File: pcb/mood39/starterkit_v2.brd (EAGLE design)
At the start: 32 x 32 mm, 19 parts, among them IC1 TINY85, IC2 LP2950

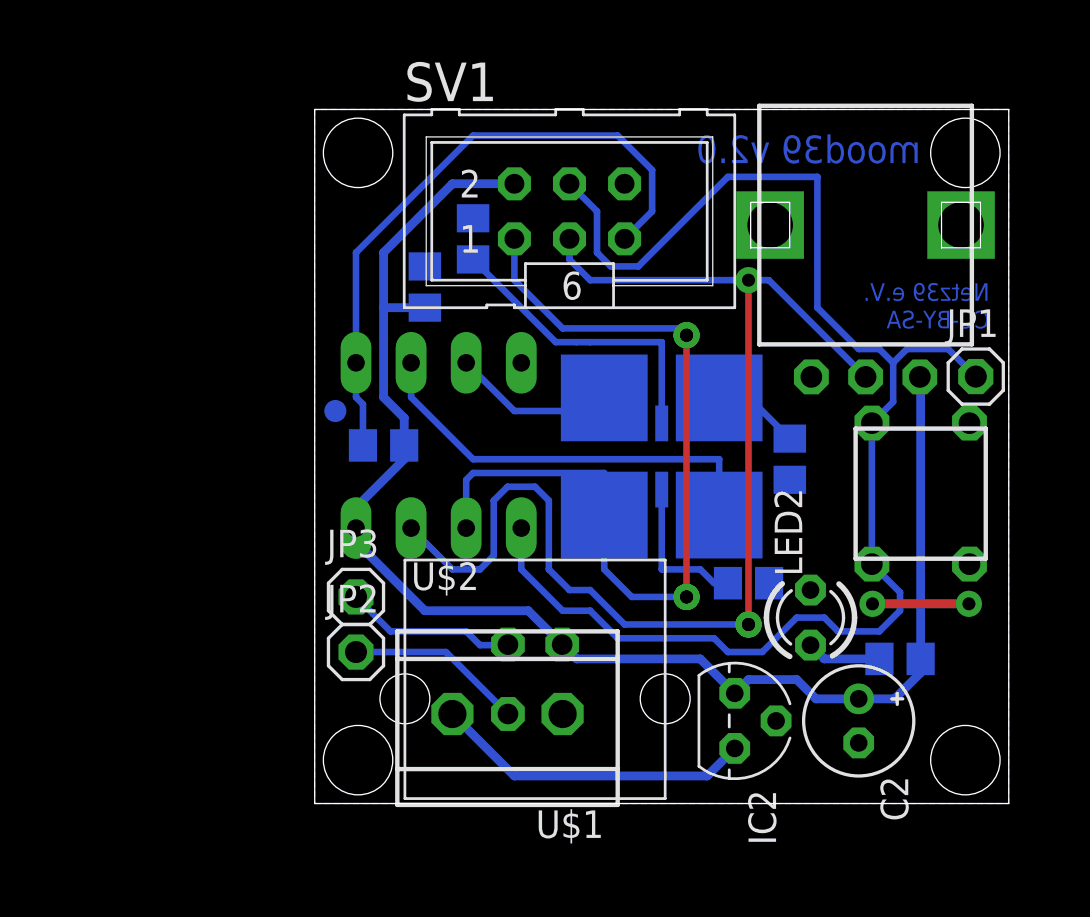
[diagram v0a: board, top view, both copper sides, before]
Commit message: move uC to top layer
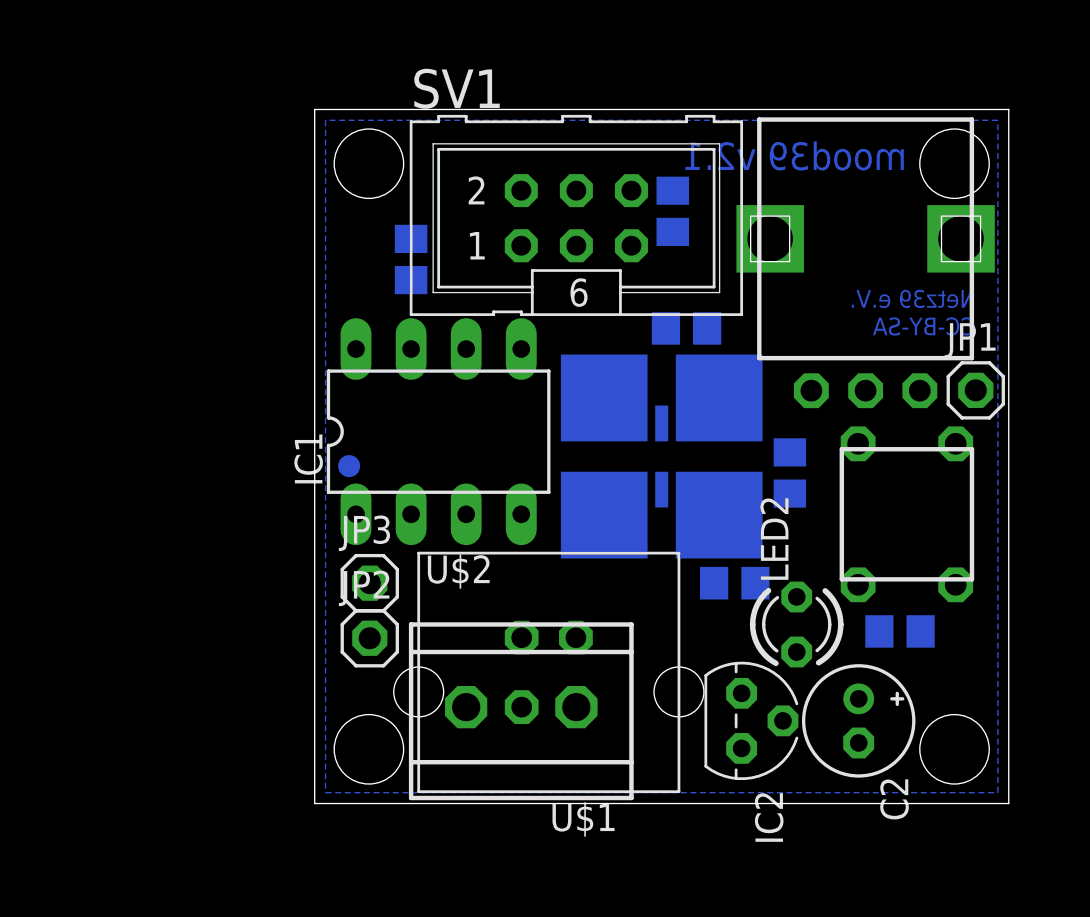
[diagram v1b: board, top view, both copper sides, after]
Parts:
- moved R1 17.2 mm to (16.5, 27.3), turned to 90 degrees
- moved R2 10.7 mm to (17.1, 21.9), turned to 180 degrees
- moved C1 1.42 mm to (4.45, 25.1)
- moved R6 1.27 mm to (27.0, 7.94)
- moved S1 1.14 mm to (27.3, 13.3)
- moved JP2 0.90 mm to (2.54, 7.62)
- moved JP3 0.90 mm to (2.54, 10.2)
- moved U$1 0.71 mm to (9.53, 4.45)
- moved U$2 0.71 mm to (10.8, 4.45)
- moved LED2 0.71 mm to (22.2, 8.26)
- moved R3 0.64 mm to (19.4, 10.2)
- moved R5 0.64 mm to (25.4, 26.0)
- moved R4 0.63 mm to (21.9, 15.2)
- moved IC1 0.63 mm to (5.71, 17.1), flipped to the top, turned to 0 degrees
- moved JP1 0.63 mm to (30.5, 19.1)
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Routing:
- net VCC: track 67.6 -> 0.00 mm
- net MOSI: track 65.6 -> 0.00 mm
- net SCK: track 56.6 -> 0.00 mm, vias 2 -> 0
- net MISO: track 41.7 -> 0.00 mm, vias 2 -> 0
- net !RESET: track 29.3 -> 0.00 mm
- net PB3: track 19.6 -> 0.00 mm
- net V+: track 14.7 -> 0.00 mm
- net N$5: track 14.0 -> 0.00 mm
- net USBD+: track 8.19 -> 0.00 mm
- net USBD-: track 7.94 -> 0.00 mm
- net PB4: track 7.54 -> 0.00 mm
- net N$6: track 7.00 -> 0.00 mm
- net GND: track 4.45 -> 0.00 mm, vias 2 -> 0
- net N$7: track 4.03 -> 0.00 mm
- net N$1: track 3.44 -> 0.00 mm
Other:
- board text added: "mood39 v2.1"
- board text removed: "mood39 v2.0"

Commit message: try another puzzle
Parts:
- moved JP1 28.6 mm to (1.91, 19.1)
- moved S1 22.9 mm to (4.45, 13.3)
- moved R6 20.7 mm to (6.99, 2.54)
- moved IC1 20.4 mm to (26.0, 15.9), turned to 180 degrees
- moved R5 18.4 mm to (6.99, 26.0)
- moved LED2 17.8 mm to (4.45, 7.62)
- moved JP2 9.44 mm to (9.53, 14.0)
- moved JP3 9.44 mm to (9.53, 16.5)
- moved SV1 8.26 mm to (20.3, 26.7)
- moved C2 5.41 mm to (28.6, 7.94), turned to 180 degrees
- moved IC2 4.45 mm to (24.1, 3.81), turned to 0 degrees
- moved C1 3.43 mm to (6.35, 22.2), turned to 0 degrees
- moved U$2 3.24 mm to (14.0, 5.08)
- moved U$1 3.24 mm to (12.7, 5.08)
- moved R1 1.27 mm to (15.2, 27.3), turned to 270 degrees
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
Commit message: new usb connector package
this will be puzzling not fun :-/
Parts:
- U$2: value USB_B -> USB_BS; device n39:USB_B_UP -> n39:USB_B_UP-S
- moved U$1 2.03 mm to (14.0, 6.67)
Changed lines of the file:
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@@
 <attribute name="REICHELT" value="TASTER 9305" x="4.445" y="13.335" size="1.778" layer="27" rot="R90" display="off"/>
 </element>
-<element name="U$1" library="n39" package="RIACON_101_2" value="RIACON_101_2" x="12.7" y="5.08" rot="R180">
-<attribute name="REICHELT" value="AKL 101-02" x="12.7" y="5.08" size="1.778" layer="27" rot="R180" display="off"/>
+<element name="U$1" library="n39" package="RIACON_101_2" value="RIACON_101_2" x="13.97" y="6.6675" rot="R180">
+<attribute name="REICHELT" value="AKL 101-02" x="13.97" y="6.6675" size="1.778" layer="27" rot="R180" display="off"/>
 </element>
 <element name="JP2" library="pinhead" package="1X01" value="" x="9.525" y="13.97"/>
 <element name="JP3" library="pinhead" package="1X01" value="" x="9.525" y="16.51"/>
-<element name="U$2" library="n39" package="USB_B_UP" value="USB_B" x="13.97" y="5.08">
+<element name="U$2" library="n39" package="USB_B_UP-S" value="USB_BS" x="13.97" y="5.08">
 <attribute name="REICHELT" value="USB BG" x="13.97" y="5.08" size="1.778" layer="27" display="off"/>
 </element>
@@
 <contactref element="U$2" pad="4"/>
 <contactref element="R5" pad="1"/>
-<wire x1="18.095" y1="22.225" x2="22.86" y2="27.94" width="0" layer="19" extent="16-16"/>
-<wire x1="22.225" y1="19.685" x2="18.095" y2="22.225" width="0" layer="19" extent="16-16"/>
-<wire x1="22.225" y1="14.925" x2="22.225" y2="19.685" width="0" layer="19" extent="16-16"/>
-<wire x1="20" y1="10.16" x2="22.225" y2="14.925" width="0" layer="19" extent="16-16"/>
-<wire x1="24.13" y1="5.715" x2="20" y2="10.16" width="0" layer="19" extent="16-16"/>
-<wire x1="27.559" y1="7.9375" x2="24.13" y2="5.715" width="0" layer="19" extent="1-1"/>
-<wire x1="15.24" y1="5.08" x2="20" y2="10.16" width="0" layer="19" extent="16-16"/>
-<wire x1="15.22" y1="5.08" x2="15.24" y2="5.08" width="0" layer="19" extent="1-1"/>
-<wire x1="6.695" y1="10.085" x2="15.24" y2="5.08" width="0" layer="19" extent="1-1"/>
-<wire x1="4.445" y1="8.89" x2="6.695" y2="10.085" width="0" layer="19" extent="1-1"/>
-<wire x1="6.695" y1="16.585" x2="6.695" y2="10.085" width="0" layer="19" extent="1-1"/>
-<wire x1="4.485" y1="19.035" x2="6.695" y2="16.585" width="0" layer="19" extent="1-1"/>
-<wire x1="5.4" y1="22.225" x2="4.485" y2="19.035" width="0" layer="19" extent="16-16"/>
 </signal>
 <signal name="VCC" class="1">
@@
 <contactref element="IC2" pad="3"/>
 <contactref element="U$1" pad="2"/>
-<wire x1="10.16" y1="5.08" x2="25.4" y2="3.81" width="0" layer="19" extent="1-1"/>
+<wire x1="11.43" y1="6.6675" x2="25.4" y2="3.81" width="0" layer="19" extent="1-1"/>
 </signal>
 <signal name="N$1" class="2">

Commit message: start routing
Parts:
- moved C1 26.2 mm to (29.2, 9.53)
- moved R1 18.5 mm to (29.8, 15.9), turned to 90 degrees
- moved R6 14.4 mm to (8.57, 16.8)
- moved JP3 11.7 mm to (1.91, 7.62)
- moved R4 8.38 mm to (17.1, 22.5), turned to 0 degrees
- moved JP2 8.13 mm to (4.45, 7.62)
- moved LED2 7.24 mm to (8.89, 13.3), turned to 270 degrees
- moved R2 3.82 mm to (13.3, 22.5), turned to 0 degrees
- moved IC2 2.03 mm to (22.5, 5.08), turned to 270 degrees
- moved C2 1.42 mm to (27.9, 6.67), turned to 270 degrees
- moved U$1 1.14 mm to (13.0, 6.03), turned to 0 degrees
- moved U$2 1.14 mm to (13.0, 4.45)
- moved S1 0.95 mm to (3.49, 13.3)
- turned SV1 to 180 degrees
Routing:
- net VCC: track 0.00 -> 54.9 mm
- net MISO: track 0.00 -> 16.6 mm
- net USBD+: track 0.00 -> 11.8 mm
- net USBD-: track 0.00 -> 10.9 mm
- net V+: track 0.00 -> 9.25 mm
- net MOSI: track 0.00 -> 9.24 mm
- net N$5: track 0.00 -> 6.73 mm
- net N$6: track 0.00 -> 6.42 mm
- net N$7: track 0.00 -> 4.40 mm
- net !RESET: track 0.00 -> 2.86 mm
- net N$1: track 0.00 -> 2.75 mm

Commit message: proceed routing, hopefully not a dead end
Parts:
- moved R3 2.54 mm to (16.5, 10.2)
- moved C1 1.85 mm to (30.2, 7.94), turned to 270 degrees
- moved R4 1.85 mm to (16.2, 24.1), turned to 90 degrees
- moved R2 1.00 mm to (14.3, 22.9), turned to 90 degrees
- moved C2 0.71 mm to (27.6, 7.30)
- moved R1 0.45 mm to (30.2, 15.6)
- moved IC1 0.45 mm to (26.4, 15.6)
- moved R6 0.45 mm to (8.89, 16.5)
- moved U$1 0.32 mm to (12.7, 6.03)
- moved U$2 0.32 mm to (12.7, 4.45)
- moved SV1 0.32 mm to (20.3, 27.0)
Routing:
- net MOSI: track 9.24 -> 51.1 mm, vias 0 -> 4
- net VCC: track 54.9 -> 22.4 mm
- net SCK: track 0.00 -> 22.3 mm
- net PB4: track 0.00 -> 17.4 mm
- net MISO: track 16.6 -> 32.8 mm, vias 0 -> 2
- net !RESET: track 2.86 -> 9.73 mm
- net N$6: track 6.42 -> 4.50 mm
- net N$7: track 4.40 -> 5.50 mm
- net N$5: track 6.73 -> 5.65 mm

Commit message: still two problems, looks like a dead end
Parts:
- moved JP3 11.7 mm to (9.53, 16.5)
- moved JP2 8.13 mm to (9.53, 14.0)
- moved LED2 7.65 mm to (3.81, 7.62)
- moved R6 3.43 mm to (6.99, 13.7), turned to 270 degrees
- moved IC2 1.27 mm to (22.5, 3.81)
- moved U$1 0.32 mm to (12.7, 5.71)
- moved U$2 0.32 mm to (12.7, 4.13)
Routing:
- net VCC: track 22.4 -> 62.1 mm
- net PB3: track 0.00 -> 23.1 mm
- net GND: track 0.00 -> 22.1 mm, vias 0 -> 7
- net MISO: track 32.8 -> 41.7 mm
- net N$1: track 2.30 -> 5.50 mm
- net !RESET: track 9.73 -> 12.1 mm
- net MOSI: track 51.1 -> 49.8 mm
- net USBD+: track 11.7 -> 12.2 mm

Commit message: no real improvement, this seemed more promising
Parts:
- moved R3 0.51 mm to (16.0, 10.2)
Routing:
- net PB3: track 23.1 -> 31.1 mm
- net MISO: track 41.7 -> 42.7 mm
- net VCC: track 62.1 -> 61.5 mm
- net GND: track 22.1 -> 22.6 mm
